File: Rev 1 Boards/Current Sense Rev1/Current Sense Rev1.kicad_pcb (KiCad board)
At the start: 2 copper layers, 32 parts, among them J1 Conn_01x02_Socket, J2 Conn_01x02_Socket, U1 TS3702, U2 INA138, U3 TLV9301xDBV, U4 TLV9301

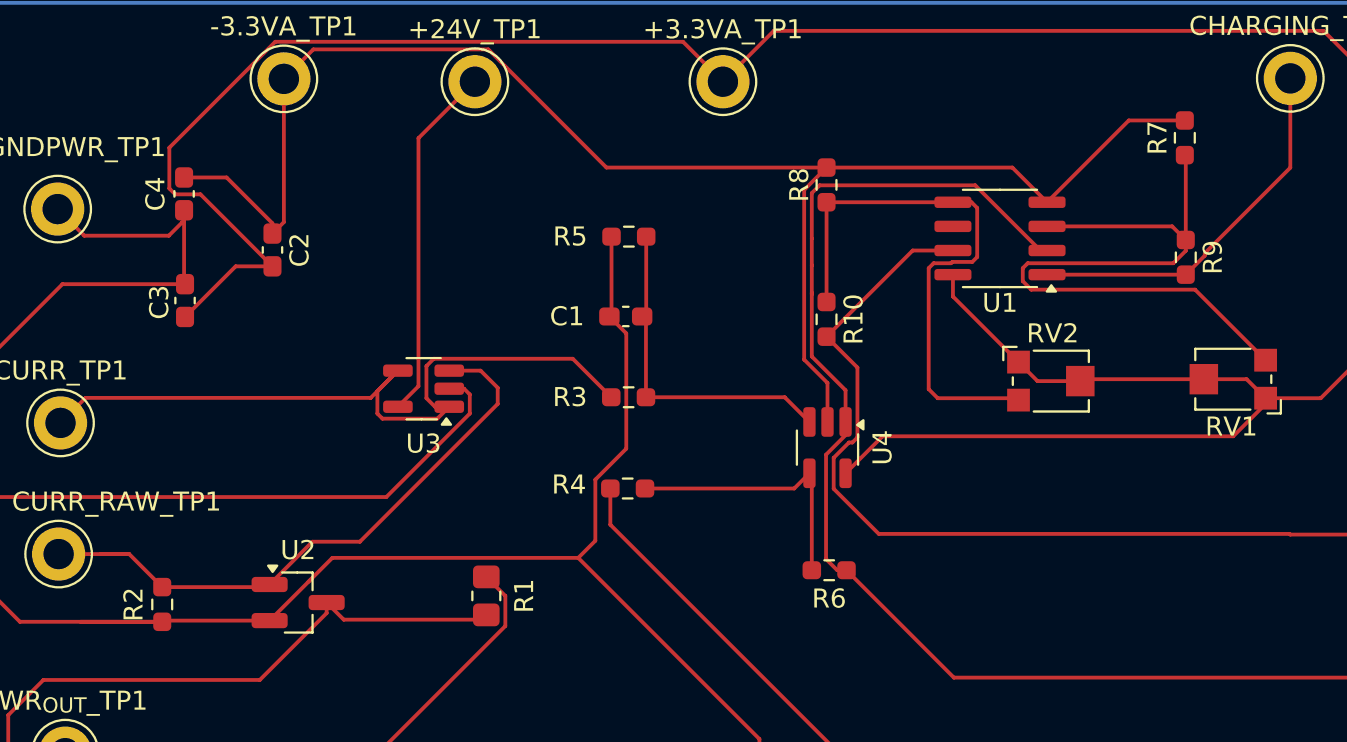
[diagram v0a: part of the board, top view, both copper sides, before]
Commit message: restore broken current sense schematic
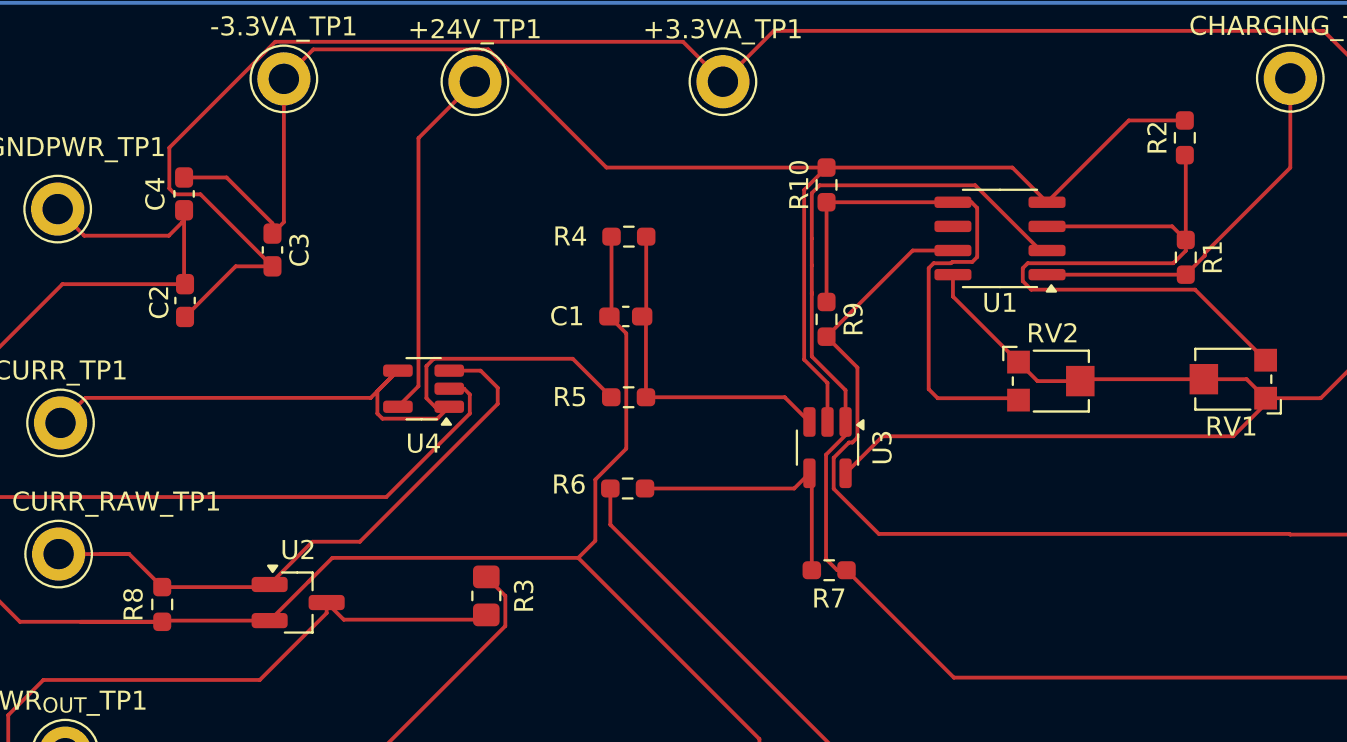
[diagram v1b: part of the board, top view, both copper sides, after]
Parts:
- removed the U3 at (169.7, 78.6)
- added U4: TLV9301, Package_TO_SOT_SMD:SOT-23-5_HandSoldering, F.Cu at (169.7, 78.6)
- C1: value 1000p -> 100p
- renumbered C3 to C2, C2 to C3, R9 to R1, R8 to R10, R7 to R2, R1 to R3, R5 to R4, R3 to R5, R4 to R6, R6 to R7, R2 to R8, R10 to R9, U4 to U3
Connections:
- U1 pad 1: /Current Sense/CHARGING_IEN -> /Current Sense/DIRECT_IEN
- U1 pad 3: /Current Sense/CEN_REF -> /Current Sense/DEN_REF
- U1 pad 5: /Current Sense/DEN_REF -> /Current Sense/CEN_REF
- U1 pad 7: /Current Sense/DIRECT_IEN -> /Current Sense/CHARGING_IEN

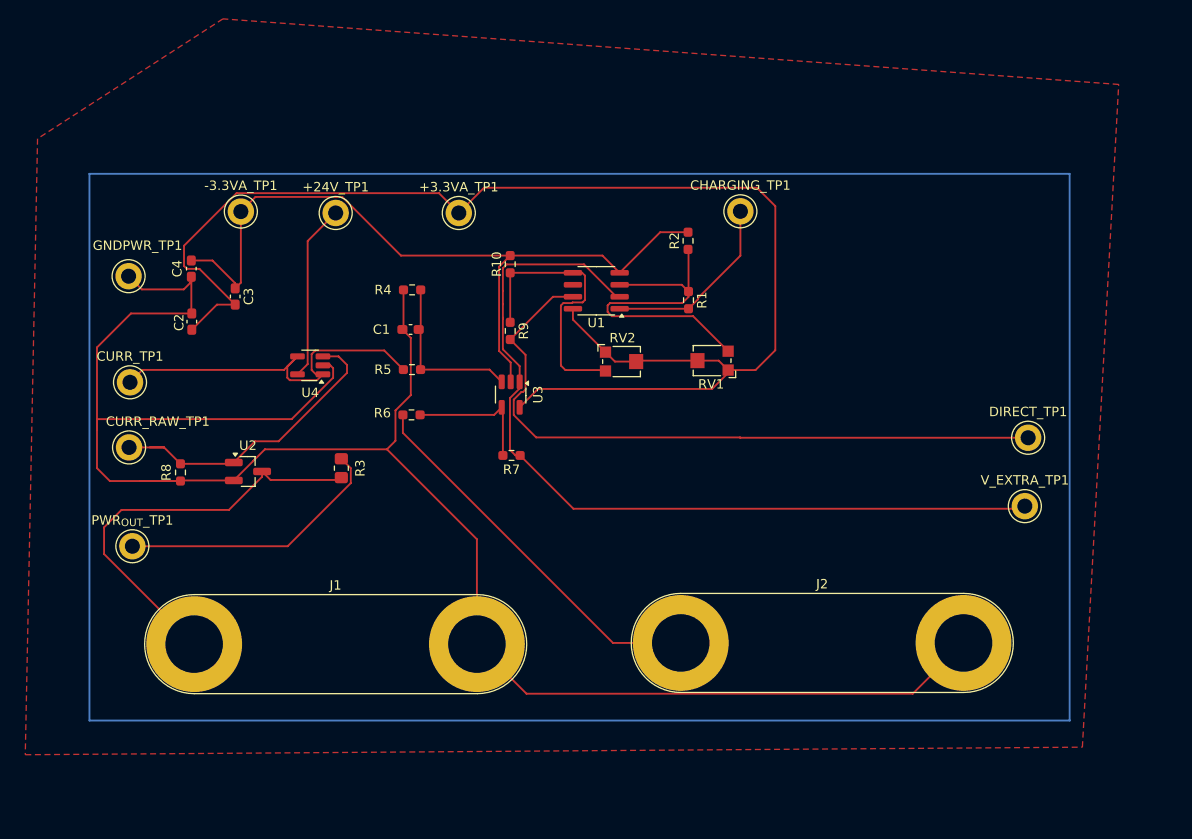
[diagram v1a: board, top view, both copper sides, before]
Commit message: current sense tweaks
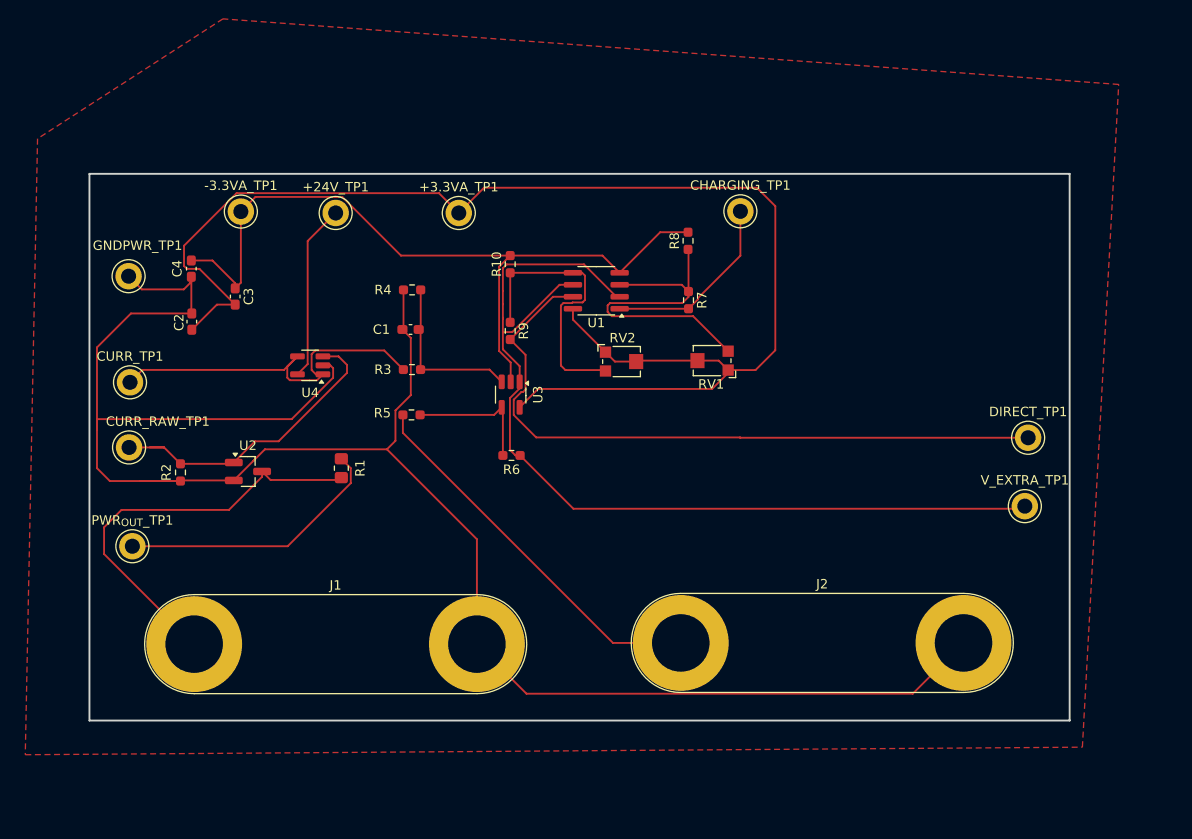
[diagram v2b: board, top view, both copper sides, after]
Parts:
- renumbered R3 to R1, R8 to R2, R5 to R3, R6 to R5, R7 to R6, R1 to R7, R2 to R8
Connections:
- U1 pad 1: /Current Sense/DIRECT_IEN -> /Current Sense/CHARGING_IEN
- U1 pad 3: /Current Sense/DEN_REF -> /Current Sense/CEN_REF
- U1 pad 5: /Current Sense/CEN_REF -> /Current Sense/DEN_REF
- U1 pad 7: /Current Sense/CHARGING_IEN -> /Current Sense/DIRECT_IEN
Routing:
- net V_EXTRA: track 91.8 -> 101.3 mm
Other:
- board outline added: 103.9 x 57.9 mm

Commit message: address current sense review issues
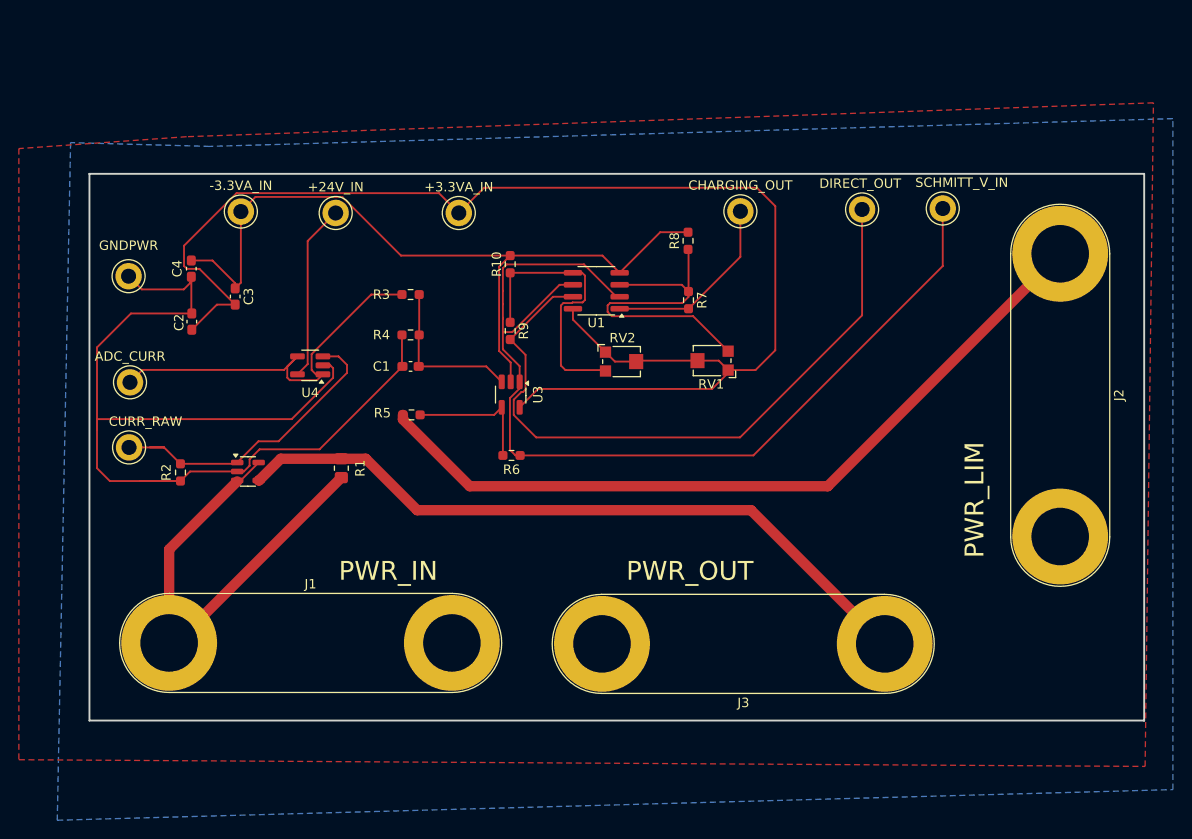
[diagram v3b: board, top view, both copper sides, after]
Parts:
- removed PWR_{OUT}_TP1: TestPoint, TestPoint:TestPoint_Keystone_5010-5014_Multipurpose
- added J3: Conn_01x02_Socket, Connector:Banana_Jack_2Pin, F.Cu at (230.6, 108.2)
- U2: footprint Package_TO_SOT_SMD:SOT-23_Handsoldering -> Package_TO_SOT_SMD:SOT-23-5
- moved J2 57.6 mm to (249.2, 66.8), turned to -90 degrees
- moved SCHMITT_V_IN 32.7 mm to (236.8, 62.0)
- moved DIRECT_OUT 29.9 mm to (228.2, 62.1)
- moved R3 7.96 mm to (180.3, 71.1)
- moved R4 4.78 mm to (180.3, 75.4)
- moved C1 3.91 mm to (180.3, 78.7)
- moved J1 2.65 mm to (154.8, 108.0)
- renumbered +24V_TP1 to +24V_IN, +3.3VA_TP1 to +3.3VA_IN, -3.3VA_TP1 to -3.3VA_IN, CURR_TP1 to ADC_CURR, CHARGING_TP1 to CHARGING_OUT, CURR_RAW_TP1 to CURR_RAW, DIRECT_TP1 to DIRECT_OUT, GNDPWR_TP1 to GNDPWR, V_EXTRA_TP1 to SCHMITT_V_IN
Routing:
- net GNDPWR: track 202.8 -> 114.4 mm
- net /Current Sense/PWR_{OUT}: track 28.9 -> 75.4 mm
- net /Current Sense/POW_LIMIT: track 40.6 -> 83.3 mm
- net /Current Sense/PWR_{IN}: track 44.7 -> 49.0 mm
- net V_EXTRA: track 101.3 -> 104.6 mm
- net /Current Sense/CURR: track 39.5 -> 41.2 mm
- net /Current Sense/DIRECT_IEN: track 73.3 -> 72.3 mm
- net /Current Sense/VN: track 17.8 -> 17.1 mm
- added copper zone on B.Cu, net GNDPWR
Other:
- board size 103.9 x 57.9 mm -> 111.8 x 57.9 mm
- board text added: "PWR_IN"
- board text added: "PWR_LIM"
- board text added: "PWR_OUT"

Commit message: modified tracks
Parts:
- moved RV1 7.42 mm to (215.3, 71.4), turned to -90 degrees
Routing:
- net /Current Sense/CEN_REF: track 36.8 -> 17.1 mm
- net +3.3VA: track 147.7 -> 132.3 mm
- net GNDPWR: track 114.4 -> 107.7 mm
- net /Current Sense/CHARGING_IEN: track 19.9 -> 21.8 mm
- net CURR_{RAW}: track 33.2 -> 31.6 mm

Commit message: review 2 revisions
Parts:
- moved J3 29.8 mm to (200.8, 108.1), turned to 0 degrees
- moved R5 13.6 mm to (191.0, 92.5), turned to 180 degrees
- moved J2 11.2 mm to (249.6, 78.0)
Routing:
- net +3.3VA: track 132.3 -> 50.8 mm, vias 0 -> 2
- net GNDPWR: track 107.7 -> 27.1 mm, vias 0 -> 3
- net -3V3: track 82.2 -> 50.4 mm
- net /Current Sense/PWR_{OUT}: track 75.4 -> 45.7 mm
- net /Current Sense/POW_LIMIT: track 83.3 -> 63.6 mm
- net /Current Sense/PWR_{IN}: track 49.0 -> 36.5 mm
- net /Current Sense/VP: track 14.1 -> 9.44 mm
- net /Current Sense/DIRECT_IEN: track 72.3 -> 70.7 mm
- added copper zone on In1.Cu, net +3.3VA
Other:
- outline, holes or cut-outs redrawn
- copper layers 2 -> 4
- board text added: "+"
- board text added: "-"
